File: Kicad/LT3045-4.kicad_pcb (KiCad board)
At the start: 4 copper layers, 100 x 50 mm, 26 parts, among them J1 Conn_Coaxial_Power, J2 Conn_Coaxial_Power, U1 LT3042, U2 LT3042, U3 LT3042, U4 LT3042

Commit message: letters and little fixes
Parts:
- moved C11 0.20 mm to (58.1, 44.1)
- moved C4 0.20 mm to (58.2, 15.0)
- moved C5 0.20 mm to (56.0, 34.8)
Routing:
- net GND: track 119.0 -> 105.6 mm, vias 1066 -> 1092
- net /VOUT: track 142.7 -> 141.8 mm
- net /VIN: track 17.0 -> 16.2 mm
- net (no net): vias 0 -> 1
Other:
- board text added: "4X LT3045 / LT3042"
- board text added: "Power Output 4xLT3045 : 0 to 15VDC @ 2000mA 4xLT3042 : 0 to 15VDC @ 800mA Noise : 0.4µVrms"
- board text added: "Power input: 1.8 to 20VDC Isolate connector ground"
- board text added: "Vset = 100µA * R3 2.5V = 25ohm 3.3V = 33ohm 5.0V = 50ohm 12V = 120ohm"

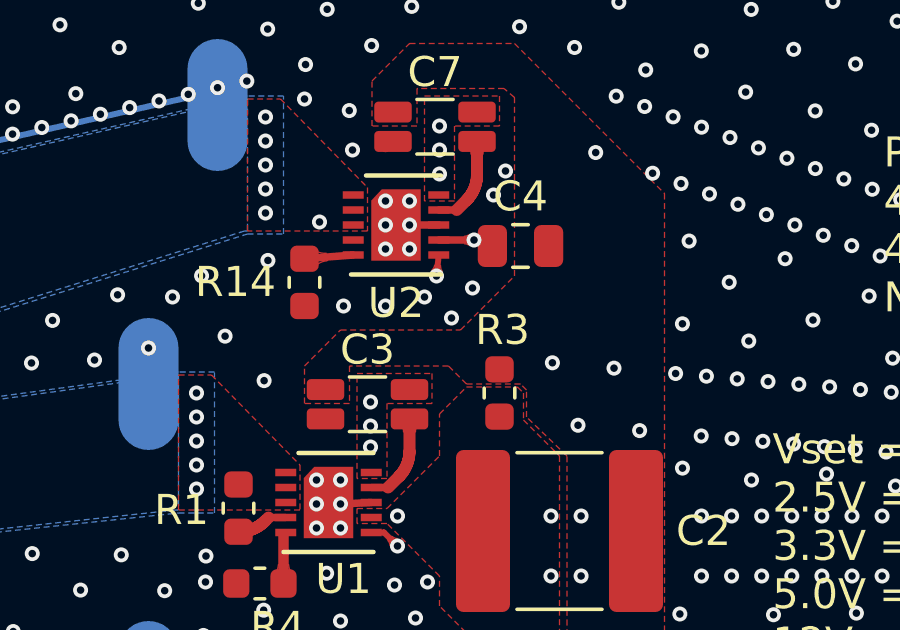
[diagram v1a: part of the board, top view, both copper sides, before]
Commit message: Input ground fix, added drill files
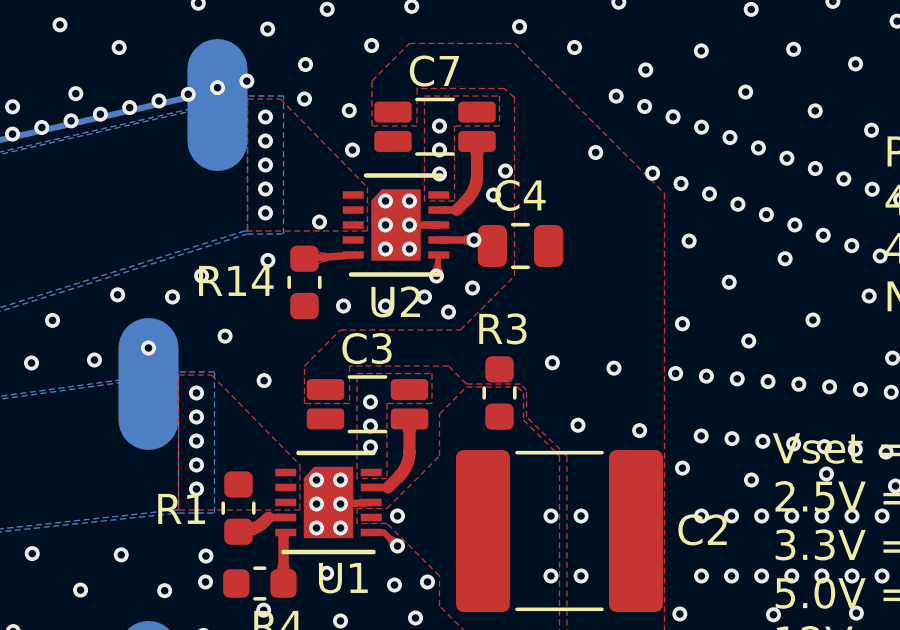
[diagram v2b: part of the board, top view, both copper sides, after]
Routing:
- net GND: vias 1092 -> 1093
- net (no net): vias 1 -> 0
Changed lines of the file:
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@@
       (padsonsilk false)
       (subtractmaskfromsilk false)
-      (outputformat 1)
+      (outputformat 4)
       (mirror false)
       (drillshape 0)
@@
   (gr_line (start 0 50) (end 100 50) (layer Edge.Cuts) (width 0.05))
   (gr_line (start 100 0) (end 100 50) (layer Edge.Cuts) (width 0.05))
-  (via (at 55 16.7) (size 0.5) (drill 0.25) (layers F.Cu B.Cu) (net 0))
+  (via (at 55 16.7) (size 0.5) (drill 0.25) (layers F.Cu B.Cu) (net 1))
   (via (at 48.101601 9.723521) (size 0.5) (drill 0.25) (layers F.Cu B.Cu) (net 1))
   (via (at 47.125285 9.944574) (size 0.5) (drill 0.25) (layers F.Cu B.Cu) (net 1))
@@
   (via (at 46.6 16.7) (size 0.5) (drill 0.25) (layers F.Cu B.Cu) (net 1))
   (via (at 53.7 17) (size 0.5) (drill 0.25) (layers F.Cu B.Cu) (net 1))
-  (via (at 55.9 17.4) (size 0.5) (drill 0.25) (layers F.Cu B.Cu) (net 1))
+  (via (at 55.8 17.2) (size 0.5) (drill 0.25) (layers F.Cu B.Cu) (net 1))
   (via (at 56.6 16.4) (size 0.5) (drill 0.25) (layers F.Cu B.Cu) (net 1))
   (via (at 52.6 11.8) (size 0.5) (drill 0.25) (layers F.Cu B.Cu) (net 1))
@@
         (xy 87.2 20.5) (xy 86.5 22.1) (xy 85.75 24.75) (xy 86.5 28) (xy 87.25 29.75)
         (xy 88.75 31.25) (xy 92.5 27.75) (xy 99.5 27.75) (xy 99.5 49.5) (xy 0.5 49.5)
-        (xy 0.5 0.5) (xy 99.5 0.5) (xy 99.5 23.8) (xy 98.1 22.2) (xy 92.6 22.2)
-        (xy 88.75 18.4)
+        (xy 0.5 31.9) (xy 12 31.9) (xy 12 18.4) (xy 0.5 18.4) (xy 0.5 0.5)
+        (xy 99.5 0.5) (xy 99.5 23.8) (xy 98.1 22.2) (xy 92.6 22.2) (xy 88.75 18.4)
       )
     )
@@
       )
     )
+  )
+  (zone (net 1) (net_name GND) (layer In2.Cu) (hatch edge 0.508)
+    (connect_pads (clearance 0.2))
+    (min_thickness 0.254)
+    (fill yes (arc_segments 32) (thermal_gap 0.508) (thermal_bridge_width 0.508))
+    (polygon
+      (pts
+        (xy 11.9 31.8) (xy 0.5 31.8) (xy 0.5 18.5) (xy 11.9 18.5)
+      )
+    )

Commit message: Lost revision :(
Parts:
- added C12: 22µF 35V, Capacitor_Tantalum_SMD:CP_EIA-7343-30_AVX-N, F.Cu at (23.2, 31.0)
- added C13: 4.7µF 35V, Capacitor_SMD:C_0805_2012Metric, F.Cu at (19.6, 22.0)
- added F1: 4A, Fuse:Fuse_Bourns_MF-SM_9.5x6.71mm, F.Cu at (12.8, 19.9)
- added L1: DLW5BTH101TQ2L, Transformer_SMD:CMC_DLW5BTH, F.Cu at (15.9, 26.3)
- added MH1: MountingHole_Pad, MountingHole:MountingHole_3.2mm_M3, F.Cu at (92.5, 7.50)
- added MH2: MountingHole_Pad, MountingHole:MountingHole_3.2mm_M3, F.Cu at (92.5, 42.5)
- added MH3: MountingHole_Pad, MountingHole:MountingHole_3.2mm_M3, F.Cu at (7.50, 7.50)
- added MH4: MountingHole_Pad, MountingHole:MountingHole_3.2mm_M3, F.Cu at (7.50, 42.5)
- added R2: 16.5k, Resistor_SMD:R_0603_1608Metric, F.Cu at (48.6, 23.6)
- added Rcdc1: Rcdc, Resistor_SMD:R_0603_1608Metric, F.Cu at (45.4, 21.9)
- RIlim1: renamed from R14; value 0 -> 287
- RIlim2: renamed from R4; value 0 -> 287
- RIlim3: renamed from R15; value 0 -> 287
- RIlim4: renamed from R16; value 0 -> 287
- moved C1 18.0 mm to (23.2, 19.0), turned to 90 degrees
- moved C10 11.5 mm to (19.6, 28.0), turned to 270 degrees
- moved L2 9.80 mm to (21.0, 25.0)
- moved C6 9.31 mm to (57.6, 20.0), turned to 0 degrees
- moved RIlim1 6.37 mm to (53.1, 10.2), turned to 180 degrees
- moved U2 5.87 mm to (57.0, 9.20)
- moved C7 5.87 mm to (58.2, 5.92)
- moved C4 5.87 mm to (61.1, 9.90)
- moved RIlim2 4.44 mm to (48.6, 21.9)
- moved U1 4.36 mm to (52.5, 19.2)
- moved C3 4.36 mm to (53.8, 16.0)
- moved R1 3.54 mm to (48.6, 20.2), turned to 180 degrees
- moved RIlim3 2.54 mm to (47.7, 33.8), turned to 180 degrees
- moved Rset1 1.80 mm to (57.4, 18.1), turned to 0 degrees
- moved RIlim4 1.44 mm to (50.2, 44.3), turned to 180 degrees
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- renumbered L1 to L2, R3 to Rset1
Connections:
- J1 pad 1: Net-(C1-Pad1) -> Net-(F1-Pad2)
- J1 pad 2: GND -> Net-(J1-Pad2)
- RIlim1 pad 2: GND -> /ILim
- RIlim2 pad 2: GND -> /ILim
- RIlim3 pad 2: GND -> /ILim
- RIlim4 pad 2: GND -> /ILim
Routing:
- net GND: track 105.6 -> 9.51 mm, vias 1093 -> 1604
- net /ILim: track 0.00 -> 41.6 mm, vias 0 -> 6
- net Net-(C1-Pad1): track 11.7 -> 0.00 mm
- net /VOUT: track 141.8 -> 131.5 mm, vias 38 -> 57
- net Net-(C11-Pad1): track 4.97 -> 12.7 mm, vias 4 -> 5
- net Net-(J1-Pad2): track 0.00 -> 2.39 mm, vias 0 -> 16
- net Net-(RIlim2-Pad1): track 1.73 -> 2.46 mm
- net /VIN: track 16.2 -> 15.8 mm, vias 36 -> 34
- added copper zone on In1.Cu, net /ILim
- added copper zone on F.Cu, net Net-(F1-Pad1)
- added copper zone on F.Cu, net Net-(F1-Pad2)
- added copper zone on B.Cu, net Net-(J1-Pad2)
- added copper zone on F.Cu, net Net-(J1-Pad2)
- added copper zone on In1.Cu, net Net-(J1-Pad2)
- added copper zone on In2.Cu, net Net-(J1-Pad2)
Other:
- board text added: "Pcdc1 = Rballast * 125 Rilim(1-4) = 150mA *kohm/Ilim -Rcdc1 * 4"
- board text added: "Philippe Trottier 2020"
- board text added: "Rbalast : 20mΩ = 1.0mm @ 0.5oz/ft² 50mΩ = 0.4mm @ 0.5oz/ft²"
- board text added: "Rbalast test: 1 mΩ 2 mΩ 3 mΩ 4 mΩ"
- board text removed: "Philippe Trottier"

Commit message: clean up
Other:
- board text added: "Rb1"
- board text added: "Rb2"
- board text added: "Rb3"
- board text added: "Rb4"
- board text added: "Rbalast test: Rb1 mΩ Rb2 mΩ Rb3 mΩ Rb4 mΩ"
- board text removed: "Rbalast test: 1 mΩ 2 mΩ 3 mΩ 4 mΩ"
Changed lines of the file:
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@@
   (general
     (thickness 1.6)
-    (drawings 60)
+    (drawings 68)
     (tracks 1954)
     (zones 0)
@@
     (visible_elements FEFFFF7F)
     (pcbplotparams
-      (layerselection 0x010f0_ffffffff)
+      (layerselection 0x010e0_ffffffff)
       (usegerberextensions false)
       (usegerberattributes true)
@@
     (tags "capacitor tantalum")
     (attr smd)
-    (fp_text reference C12 (at 0 -3.1 90) (layer F.SilkS)
+    (fp_text reference C12 (at 2.0875 -3.2 90) (layer F.SilkS)
       (effects (font (size 1 1) (thickness 0.15)))
     )
@@
       (effects (font (size 1 1) (thickness 0.15)))
     )
-    (pad 1 smd roundrect (at -3.1125 0 270) (size 2.075 2.55) (layers F.Cu F.Paste F.Mask) (roundrect_rratio 0.120482)
+    (pad 1 smd roundrect (at -3.1125 0 270) (size 2.075 2.55) (layers F.Cu F.Paste F.Mask) (roundrect_rratio 0.1204819277108434)
       (net 2 "Net-(C1-Pad1)"))
-    (pad 2 smd roundrect (at 3.1125 0 270) (size 2.075 2.55) (layers F.Cu F.Paste F.Mask) (roundrect_rratio 0.120482)
+    (pad 2 smd roundrect (at 3.1125 0 270) (size 2.075 2.55) (layers F.Cu F.Paste F.Mask) (roundrect_rratio 0.1204819277108434)
       (net 1 GND))
     (model ${KISYS3DMOD}/Capacitor_Tantalum_SMD.3dshapes/CP_EIA-7343-30_AVX-N.wrl
@@
     )
   )
-  (gr_poly (pts (xy 38 30.5) (xy 29.3 30.5) (xy 29.3 28) (xy 38 28)) (layer F.SilkS) (width 0.1))
-  (gr_poly (pts (xy 38 27.2) (xy 29.3 27.2) (xy 29.3 24.7) (xy 38 24.7)) (layer F.SilkS) (width 0.1))
-  (gr_poly (pts (xy 38 23.9) (xy 29.3 23.9) (xy 29.3 21.4) (xy 38 21.4)) (layer F.SilkS) (width 0.1))
-  (gr_poly (pts (xy 38 20.6) (xy 29.3 20.6) (xy 29.3 18.1) (xy 38 18.1)) (layer F.SilkS) (width 0.1))
-  (gr_text "Rbalast test:\n\n1             mΩ\n\n2             mΩ\n\n3             mΩ\n\n4             mΩ" (at 27.7 23.3) (layer F.SilkS)
+  (gr_text Rb2 (at 60.5 15.5) (layer F.SilkS)
+    (effects (font (size 1 1) (thickness 0.15)))
+  )
+  (gr_text Rb3 (at 59.5 29) (layer F.SilkS)
+    (effects (font (size 1 1) (thickness 0.15)))
+  )
+  (gr_text Rb4 (at 62.1 39.5) (layer F.SilkS)
+    (effects (font (size 1 1) (thickness 0.15)))
+  )
+  (gr_text Rb4 (at 89.5 29.5) (layer F.SilkS)
+    (effects (font (size 1 1) (thickness 0.15)))
+  )
+  (gr_text Rb3 (at 88.8 27) (layer F.SilkS)
+    (effects (font (size 1 1) (thickness 0.15)))
+  )
+  (gr_text Rb2 (at 88.8 23.2) (layer F.SilkS)
+    (effects (font (size 1 1) (thickness 0.15)))
+  )
+  (gr_text Rb1 (at 89.6 20.8) (layer F.SilkS)
+    (effects (font (size 1 1) (thickness 0.15)))
+  )
+  (gr_text Rb1 (at 62.2 3.8) (layer F.SilkS)
+    (effects (font (size 1 1) (thickness 0.15)))
+  )
+  (gr_poly (pts (xy 38.8 30.5) (xy 30.1 30.5) (xy 30.1 28) (xy 38.8 28)) (layer F.SilkS) (width 0.1))
+  (gr_poly (pts (xy 38.8 27.2) (xy 30.1 27.2) (xy 30.1 24.7) (xy 38.8 24.7)) (layer F.SilkS) (width 0.1))
+  (gr_poly (pts (xy 38.8 23.9) (xy 30.1 23.9) (xy 30.1 21.4) (xy 38.8 21.4)) (layer F.SilkS) (width 0.1))
+  (gr_poly (pts (xy 38.8 20.6) (xy 30.1 20.6) (xy 30.1 18.1) (xy 38.8 18.1)) (layer F.SilkS) (width 0.1))
+  (gr_text "Rbalast test:\n\nRb1            mΩ\n\nRb2            mΩ\n\nRb3            mΩ\n\nRb4            mΩ" (at 27 23.3) (layer F.SilkS)
     (effects (font (size 1 1) (thickness 0.15)) (justify left))
   )

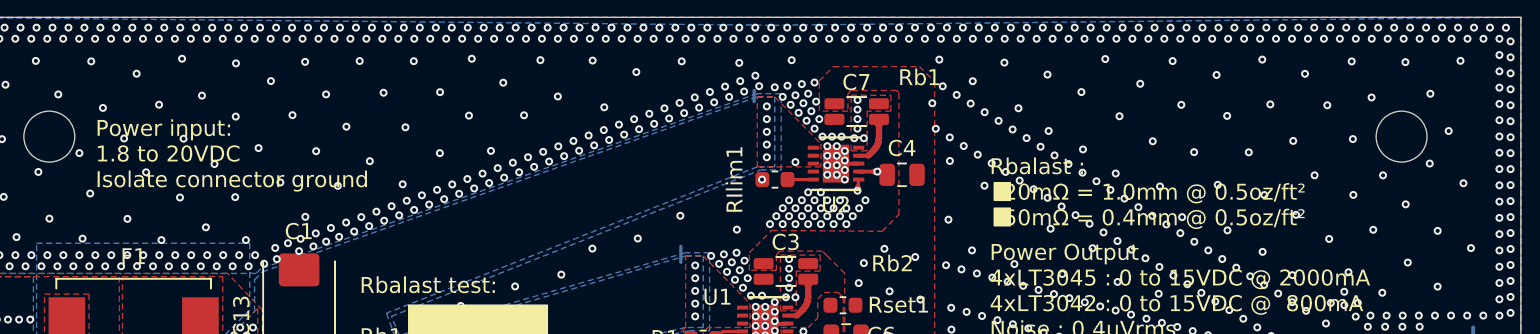
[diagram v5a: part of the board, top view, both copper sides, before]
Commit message: line width mistake corrected on silk screen
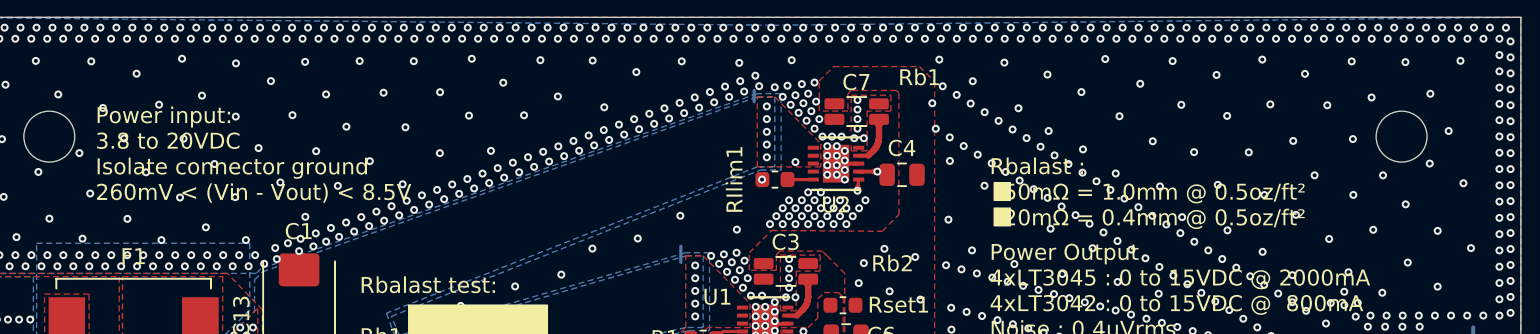
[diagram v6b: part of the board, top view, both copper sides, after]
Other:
- board text added: "Power input: 3.8 to 20VDC Isolate connector ground 260mV < (Vin - Vout) < 8.5V"
- board text added: "Rbalast : 50mΩ = 1.0mm @ 0.5oz/ft² 20mΩ = 0.4mm @ 0.5oz/ft²"
- board text removed: "Power input: 1.8 to 20VDC Isolate connector ground"
- board text removed: "Rbalast : 20mΩ = 1.0mm @ 0.5oz/ft² 50mΩ = 0.4mm @ 0.5oz/ft²"
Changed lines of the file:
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@@
       (padsonsilk false)
       (subtractmaskfromsilk false)
-      (outputformat 4)
+      (outputformat 1)
       (mirror false)
       (drillshape 0)
@@
   (gr_poly (pts (xy 67.9 13.1) (xy 66.9 13.1) (xy 66.9 12) (xy 67.9 12)) (layer F.SilkS) (width 0.1))
   (gr_poly (pts (xy 67.9 11.5) (xy 66.9 11.5) (xy 66.9 10.4) (xy 67.9 10.4)) (layer F.SilkS) (width 0.1))
-  (gr_text "Rbalast :\n  20mΩ = 1.0mm @ 0.5oz/ft²\n  50mΩ = 0.4mm @ 0.5oz/ft²" (at 66.6 11) (layer F.SilkS)
+  (gr_text "Rbalast :\n  50mΩ = 1.0mm @ 0.5oz/ft²\n  20mΩ = 0.4mm @ 0.5oz/ft²" (at 66.6 11) (layer F.SilkS)
     (effects (font (size 1 1) (thickness 0.15)) (justify left))
   )
@@
     (effects (font (size 1 1) (thickness 0.15)) (justify left))
   )
-  (gr_text "Power input:\n1.8 to 20VDC\nIsolate connector ground" (at 10.4 8.6) (layer F.SilkS)
+  (gr_text "Power input:\n3.8 to 20VDC\nIsolate connector ground\n260mV < (Vin - Vout) < 8.5V" (at 10.4 8.6) (layer F.SilkS)
     (effects (font (size 1 1) (thickness 0.15)) (justify left))
   )

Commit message: 1st LNA
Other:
- board text added: "Power input: 3.8 to 20VDC Isolate connector ground LT3045 260mV < (Vin - Vout) < 8.5V LT3042 350mV < (Vin - Vout) < 8.5V"
- board text removed: "Power input: 3.8 to 20VDC Isolate connector ground 260mV < (Vin - Vout) < 8.5V"
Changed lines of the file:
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@@
     (effects (font (size 1 1) (thickness 0.15)) (justify left))
   )
-  (gr_text "Power input:\n3.8 to 20VDC\nIsolate connector ground\n260mV < (Vin - Vout) < 8.5V" (at 10.4 8.6) (layer F.SilkS)
+  (gr_text "Power input:\n3.8 to 20VDC\nIsolate connector ground\nLT3045 260mV < (Vin - Vout) < 8.5V\nLT3042 350mV < (Vin - Vout) < 8.5V" (at 10.4 8.6) (layer F.SilkS)
     (effects (font (size 1 1) (thickness 0.15)) (justify left))
   )
